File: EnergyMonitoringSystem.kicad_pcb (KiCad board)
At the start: 6 copper layers, 170 x 114.4 mm, 205 parts, among them J201 USB_C_Receptacle_USB2.0_16P, J202 Screw_Terminal_01x02, J401 Conn_02x05_Counter_Clockwise, J402 Conn_02x05_Counter_Clockwise, J403 Conn_02x08_Counter_Clockwise, J501 Screw_Terminal_01x02, J502 Screw_Terminal_01x02, J503 Screw_Terminal_01x02, J504 Screw_Terminal_01x02, J505 Screw_Terminal_01x02, J506 Screw_Terminal_01x02, J601 DM3AT-SF-PEJM5_40_, J602 Screw_Terminal_01x03, Q201 STL6N3LLH6, SW401 SW_Push, SW402 SW_Push, U201 USBLC6-2P6, U202 STEF05SGR, U203 TCPP01-M12, U301 LDLN025M12R, U302 ST1PS02CQTR, U303 ST1PS02CQTR, U304 LM2664M6_NOPB, U401 STM32F103RGT6, U402 BLUENRG-M2SA, U501 ADS131M08IRSNR, U502 TSV914AIDR, U503 TSV914AIDR, U504 TSV914AIDR, U601 EMIF06-MSD02N16, U602 ADM2565EBRNZ, Y401 16MHz, Y402 32.768KHz

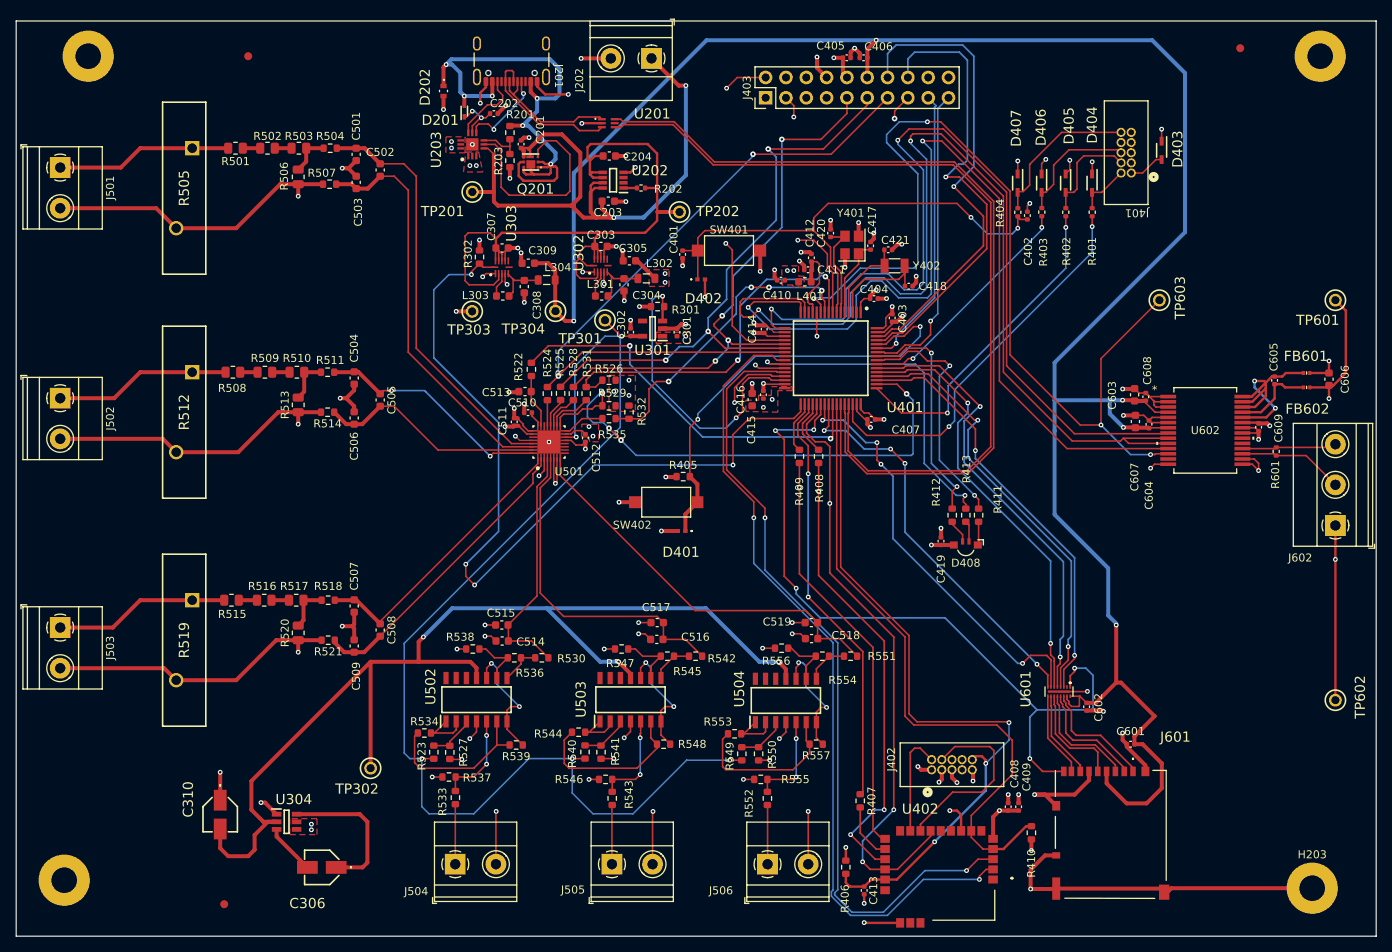
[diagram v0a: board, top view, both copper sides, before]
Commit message: erc with no error
1. Updated footprint for ADS
2. fixed constraints
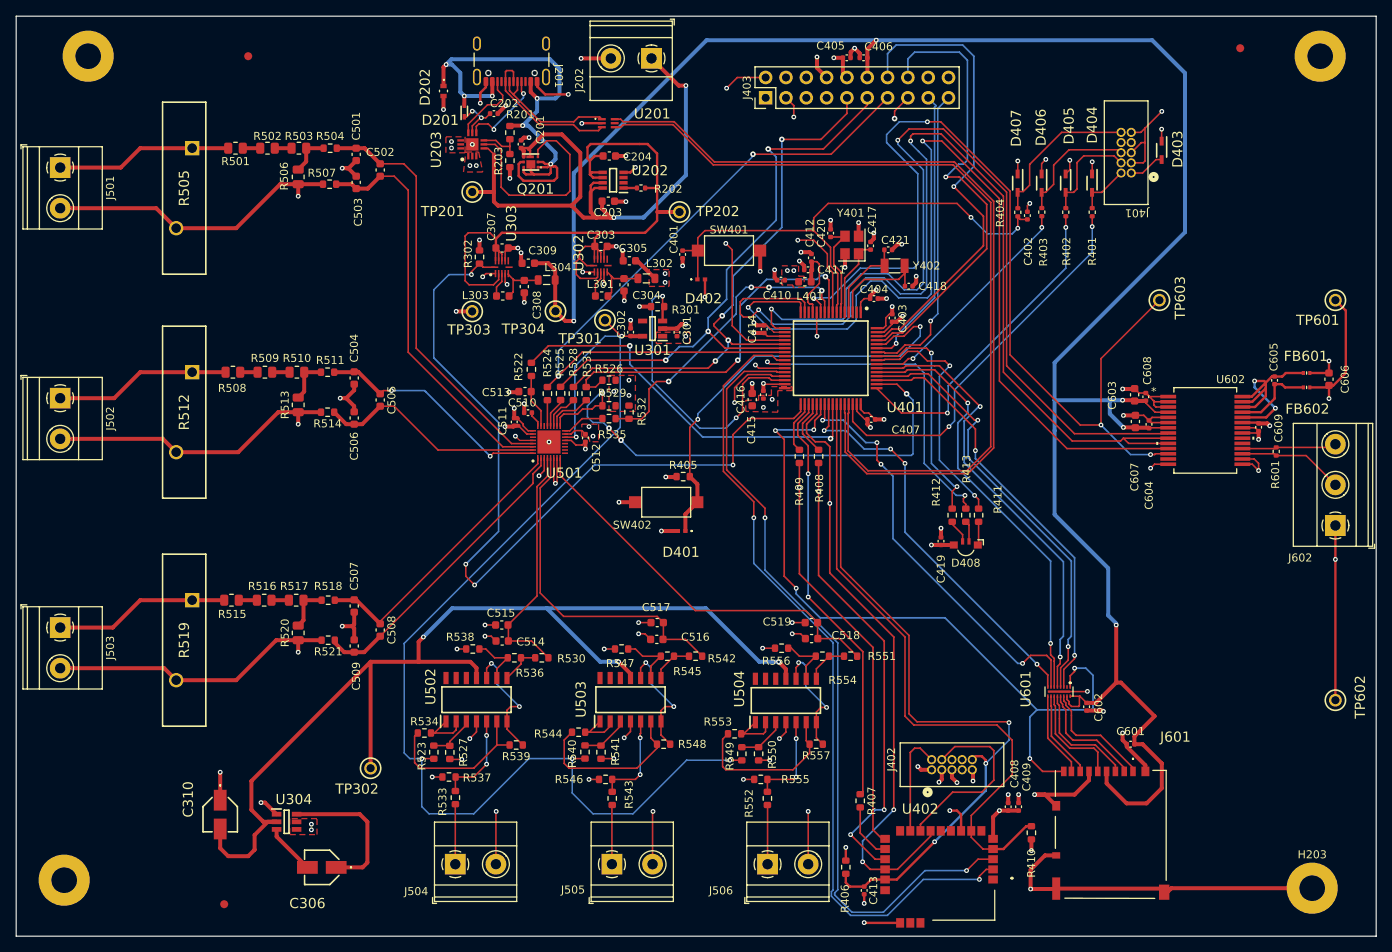
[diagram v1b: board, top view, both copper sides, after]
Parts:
- U501: footprint EMS:ADS131M08IPBS-WQFN-A -> EMS:ADS131M08IRSNR-QFN40
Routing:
- net GND: track 410.6 -> 423.6 mm, vias 111 -> 112
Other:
- board size 170 x 114.4 mm -> 170 x 115 mm

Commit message: minor updates
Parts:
- moved J505 3.42 mm to (104.8, 147.4)
- moved J506 3.40 mm to (123.8, 147.4)
- moved J504 3.40 mm to (84.8, 147.4)
- moved R409 0.84 mm to (127.1, 93.3)
- moved R408 0.70 mm to (129.6, 93.0)
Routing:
- net GND: track 423.6 -> 434.1 mm
- net Net-(J505-Pin_1): track 7.41 -> 11.0 mm
- net Net-(J506-Pin_1): track 7.41 -> 10.8 mm
- net Net-(J504-Pin_1): track 7.51 -> 10.9 mm
- net /uC/SPI2_MOSI: track 125.0 -> 126.2 mm
- net ADS_CS: track 114.4 -> 113.5 mm
- net ADS_STM32_CLKOUT: track 48.9 -> 49.7 mm

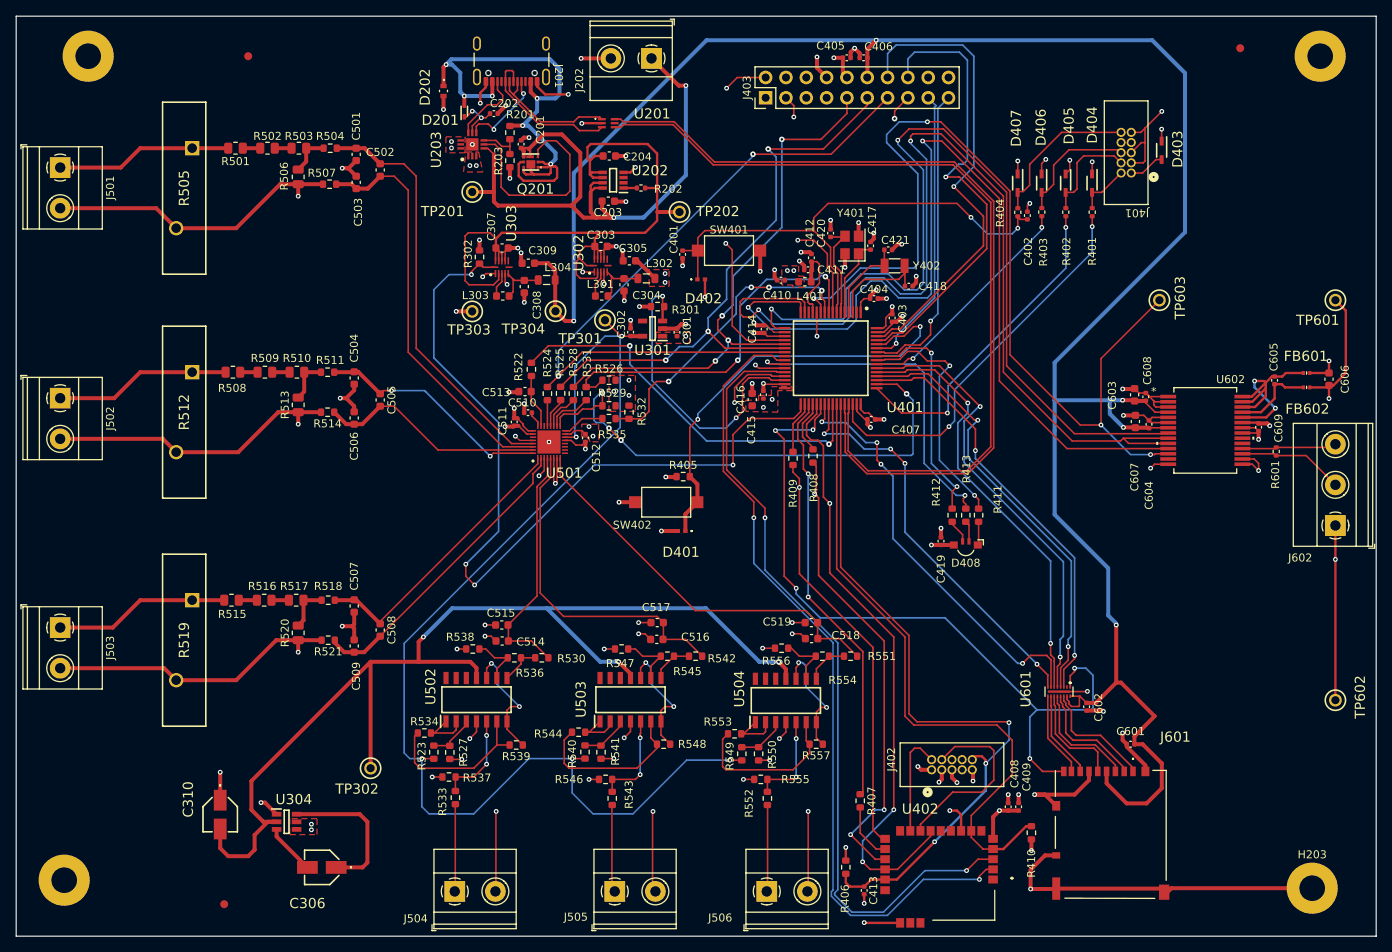
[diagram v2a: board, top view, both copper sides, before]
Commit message: added some silkscreen texts and logos
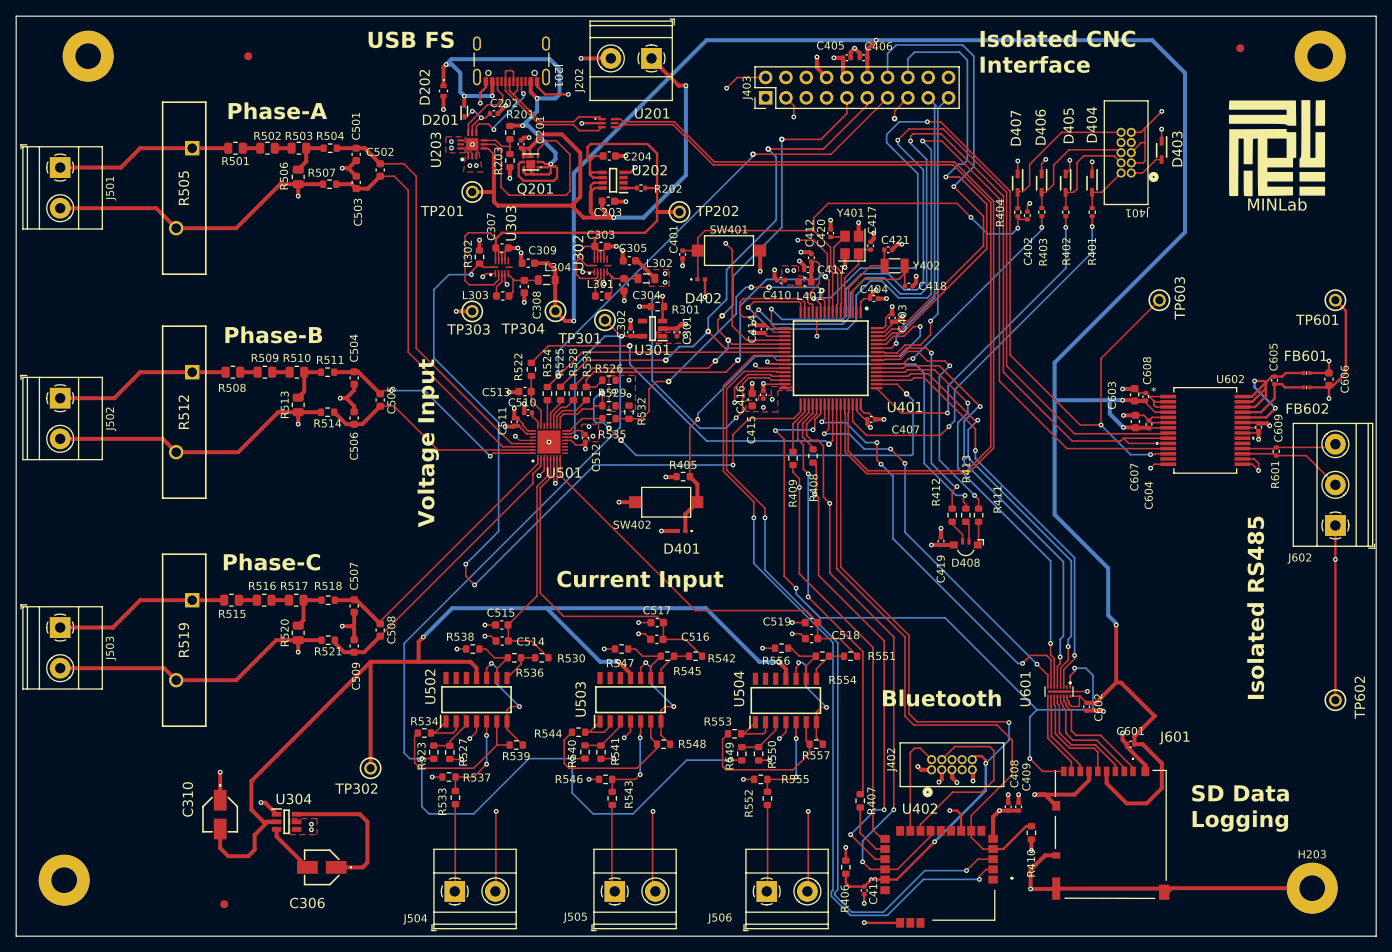
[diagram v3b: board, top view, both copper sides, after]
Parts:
- added G***: MINLab, LOGO, F.Cu at (187.6, 54.5)
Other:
- board text added: "Bluetooth"
- board text added: "Current Input"
- board text added: "Isolated CNC Interface"
- board text added: "Isolated RS485"
- board text added: "Phase-A"
- board text added: "Phase-B"
- board text added: "Phase-C"
- board text added: "SD Data Logging"
- board text added: "USB FS"
- board text added: "Voltage Input"
